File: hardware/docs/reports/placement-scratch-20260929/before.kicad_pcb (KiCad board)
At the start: 4 copper layers, 99.4 x 61 mm, 144 parts, among them J3 TFT032B018, J4 SolderWire-1.5sqmm, J7 USB_C_Receptacle_USB2.0_16P, J8 2-CH UART TO ETH, J9 ENCODER CABLE, Q1 BSS138P, Q2 BSS138P, Q3 SQJB60EP, Q4 BSS138P, Q5 SQJB60EP, Q6 BSS138P, Q7 IRLML6344, Q8 TSM3443CX6, SW1 BOOT / PTS810, SW2 RESET / PTS810, U1 AP33772SDKZ-13-FA02, U10 USBLC6-2SC6, U11 TPS55340PWPR, U12 LM74801-Q1, U13 74LVC1G08, U2 ESP32-C6-MINI-1-H4, U3 INA226, U4 BQ32000, U5 AOZ1284PI, U6 TLV431BQDBZT, Y1 32.768kHz

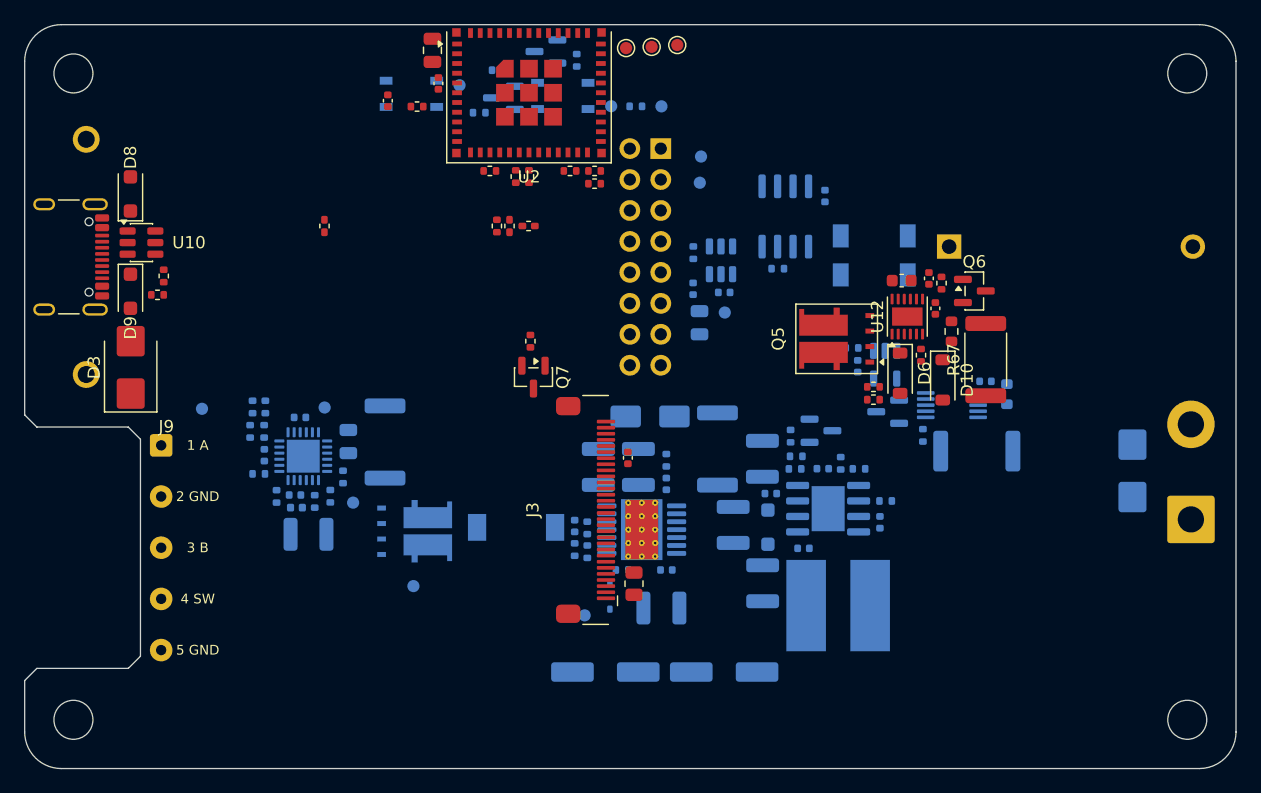
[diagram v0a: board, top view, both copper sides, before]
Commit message: REV_C yerlesim: agirlikli ratsnest araclari, FPC keepout, routability ve ESP32 pin atamasi
Yerlesim (hardware/gopo.kicad_pcb, kilitli H1-H4/J3 yerinde, parite 0):
- TASK-115: kilitsiz parcalarin agirlikli ratsnest ile sifirdan yerlesimi
- TASK-118: agirlik 10/5/5 (W_ORDINARY) ve LCD FPC bukum yolunda top'ta parca yok
- TASK-119: kesisme cezasi, dekuplaj-IC ayni yuz kurali (flip destegi), IC-yerel kenarlar
- TASK-122: In2 guc polygonlari metrige yansidi (PLANE_NETS), sinyal kesismesi 75 -> 51
- TASK-124: BOOST LNS (sicak dongu sabit), C23 SS 7.0 -> 2.7 mm; PD degismedi

ESP32-C6 pin atamasi (TASK-123, kullanici onayli):
- mcu.kicad_sch: U2 pinlerindeki 12 etiket yeniden adlandirildi; ERC 0, netlist
  farki yalniz bu netler. Sinyal kesismesi 51 -> 38.
- FIRMWARE_GEREKSINIMLERI.md pin tablosu; TASK-033 I2C GPIO22/23.

Araclar:
- kicad-placement skill: placelib/place.py (anneal/legal/refine/sweep/untangle/align,
  LNS --blocks), pcb_dump/apply/check/render, pcb_freeroute (TASK-120 deneme routing)
- update_pcb.py: board-only ve kilitli footprint'ler artik silinmiyor (H1-H4, MECH_ENC)

Kararlar: design_decisions/output/SIFIRDAN_YERLESIM_AGIRLIKLI_RATSNEST_20260929.md
Acik isler: TASK-116 (serigrafi), TASK-117, TASK-121.

Co-Authored-By: Claude Opus 5.5 <noreply@anthropic.com>
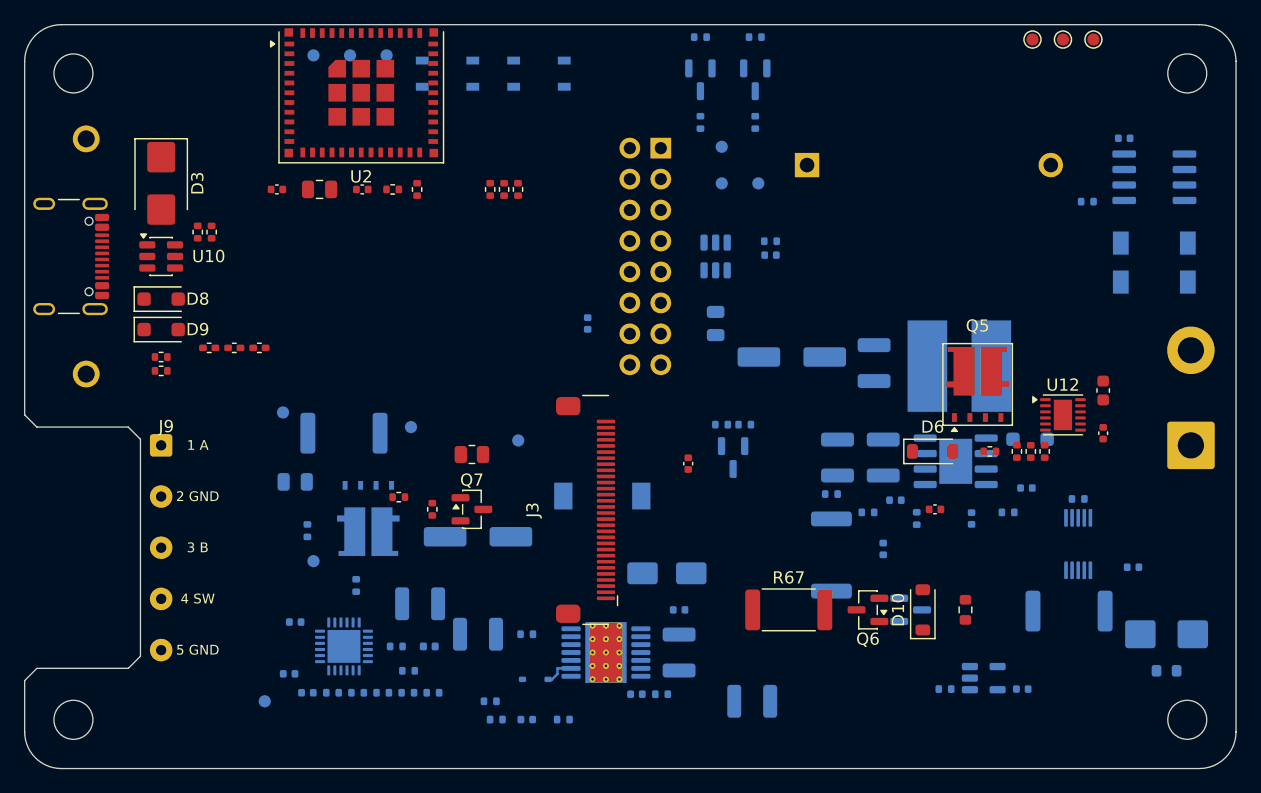
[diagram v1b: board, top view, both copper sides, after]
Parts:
- moved TP13 34.2 mm to (138.0, 70.7), turned to 0 degrees
- moved TP12 33.8 mm to (135.5, 70.7), turned to 0 degrees
- moved TP11 33.4 mm to (133.0, 70.7), turned to 0 degrees
- moved U4 30.5 mm to (143.0, 82.0), turned to 180 degrees
- moved C35 29.7 mm to (132.2, 124.0), turned to 0 degrees
- moved R61 29.0 mm to (125.8, 124.0)
- moved TP6 28.9 mm to (74.0, 72.0), turned to 0 degrees
- moved R9 27.7 mm to (83.8, 124.3), turned to 180 degrees
- moved Q6 27.6 mm to (119.5, 117.5), turned to 180 degrees
- moved U13 27.0 mm to (129.0, 123.1), turned to 0 degrees
- moved R2 26.5 mm to (64.5, 86.5)
- moved R3 26.4 mm to (65.6, 86.5)
- moved C15 26.4 mm to (113.2, 96.8), turned to 180 degrees
- moved R59 26.2 mm to (144.0, 122.5), turned to 0 degrees
- moved R67 26.1 mm to (113.0, 117.5), turned to 0 degrees
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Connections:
- U2 pad 10: TFT_DC -> TFT_MOSI
- U2 pad 16: ENCODER_B -> TFT_DC
- U2 pad 19: ENCODER_SW -> TFT_CS
- U2 pad 20: TFT_CS -> TFT_RST
- U2 pad 24: TFT_MOSI -> PD_I2C_SCL_3V3
- U2 pad 25: TFT_RST -> PD_I2C_SDA_3V3
- U2 pad 26: INA_ALERT -> PD_INT_3V3
- U2 pad 27: /MCU/RTC_INT -> ENCODER_SW
- U2 pad 28: PD_I2C_SCL_3V3 -> ENCODER_A
- U2 pad 29: PD_I2C_SDA_3V3 -> ENCODER_B
- U2 pad 5: PD_INT_3V3 -> /MCU/RTC_INT
- U2 pad 6: ENCODER_A -> INA_ALERT
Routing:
- net /USB_PD_CONTROLLER/BOOST_FB: track 0.00 -> 2.58 mm
